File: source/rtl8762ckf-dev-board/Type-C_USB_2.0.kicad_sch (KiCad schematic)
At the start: 14 parts, among them J10 USB_C_Receptacle_USB2.0, U3 USBLC6-2SC6

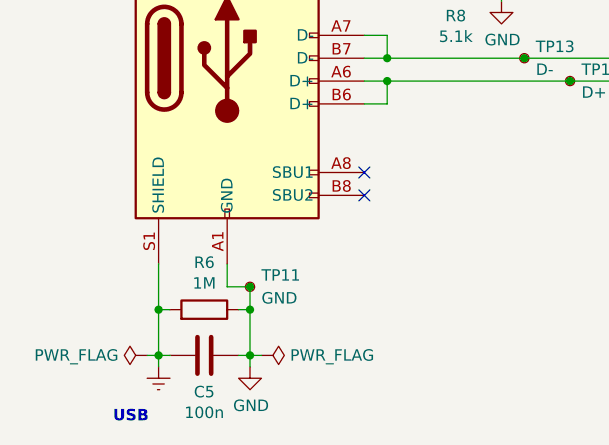
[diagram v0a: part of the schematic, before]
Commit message: implemented pico probe
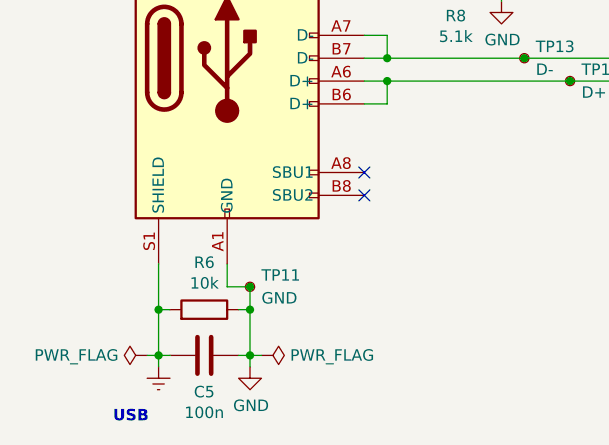
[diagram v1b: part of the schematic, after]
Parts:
- C5, C6: LCSC (none) -> C1546; MPN (none) -> 0402CG101J500NT
- C7: LCSC (none) -> C15525; MPN (none) -> CL05A106MQ5NUNC
- F1: LCSC C914092 -> C124083; MPN BSMD0603-075-6V -> BSMD0402L-050
- FB1: footprint Inductor_SMD:L_0402_1005Metric -> Inductor_SMD:L_0603_1608Metric; MPN UPZ1608E601-2R0TF -> CBW100505U601T
- J10: LCSC C2848615 -> C2927039; MPN TYPE-C-31-D-09 -> USB-TYPE-C-019
- R6: value 1M -> 10k; LCSC (none) -> C25086; MPN (none) -> 0402WGF100KTCE
- R7, R8: LCSC (none) -> C25905; MPN (none) -> 0402WGF5101TCE
- U3: LCSC (none) -> C2687116; MPN (none) -> USBLC6-2SC6
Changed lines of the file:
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@@
       (project "rtl8762ckf-dev-board"
         (path "/5477044b-5ae5-4ed6-bb7d-f5f3cc95a2d4/b26c93f0-3164-4866-a133-0e94099f2b64"
-          (reference "#PWR010") (unit 1)
+          (reference "#PWR027") (unit 1)
         )
       )
@@
       (effects (font (size 1.27 1.27)) hide)
     )
-    (property "Datasheet" "https://www.usb.org/sites/default/files/documents/usb_type-c.zip" (at 39.37 43.18 0)
-      (effects (font (size 1.27 1.27)) hide)
-    )
-    (property "LCSC" "C2848615" (at 35.56 43.18 0)
-      (effects (font (size 1.27 1.27)) hide)
-    )
-    (property "MPN" "TYPE-C-31-D-09" (at 35.56 43.18 0)
+    (property "Datasheet" "https://datasheet.lcsc.com/lcsc/2201121330_DEALON-USB-TYPE-C-019_C2927039.pdf" (at 39.37 43.18 0)
+      (effects (font (size 1.27 1.27)) hide)
+    )
+    (property "LCSC" "C2927039" (at 35.56 43.18 0)
+      (effects (font (size 1.27 1.27)) hide)
+    )
+    (property "MPN" "USB-TYPE-C-019" (at 35.56 43.18 0)
       (effects (font (size 1.27 1.27)) hide)
     )
@@
       (project "rtl8762ckf-dev-board"
         (path "/5477044b-5ae5-4ed6-bb7d-f5f3cc95a2d4/b26c93f0-3164-4866-a133-0e94099f2b64"
-          (reference "J2") (unit 1)
+          (reference "J7") (unit 1)
         )
       )
@@
       (effects (font (size 1.27 1.27)) hide)
     )
-    (property "Datasheet" "http://www2.st.com/resource/en/datasheet/CD00050750.pdf" (at 100.33 53.34 0)
+    (property "Datasheet" "http://www2.st.com/resource/en/datasheet/CD00050750.https://datasheet.lcsc.com/lcsc/2206231215_UMW-Youtai-Semiconductor-Co---Ltd--USBLC6-2SC6_C2687116.pdf" (at 100.33 53.34 0)
+      (effects (font (size 1.27 1.27)) hide)
+    )
+    (property "LCSC" "C2687116" (at 109.22 58.42 0)
+      (effects (font (size 1.27 1.27)) hide)
+    )
+    (property "MPN" "USBLC6-2SC6" (at 109.22 58.42 0)
       (effects (font (size 1.27 1.27)) hide)
     )
@@
       (project "rtl8762ckf-dev-board"
         (path "/5477044b-5ae5-4ed6-bb7d-f5f3cc95a2d4/b26c93f0-3164-4866-a133-0e94099f2b64"
-          (reference "U2") (unit 1)
+          (reference "U3") (unit 1)
         )
       )
@@
       (project "rtl8762ckf-dev-board"
         (path "/5477044b-5ae5-4ed6-bb7d-f5f3cc95a2d4/b26c93f0-3164-4866-a133-0e94099f2b64"
-          (reference "#PWR013") (unit 1)
+          (reference "#PWR030") (unit 1)
         )
       )
@@
       (project "rtl8762ckf-dev-board"
         (path "/5477044b-5ae5-4ed6-bb7d-f5f3cc95a2d4/b26c93f0-3164-4866-a133-0e94099f2b64"
-          (reference "#PWR08") (unit 1)
+          (reference "#PWR025") (unit 1)
         )
       )
@@
       (project "rtl8762ckf-dev-board"
         (path "/5477044b-5ae5-4ed6-bb7d-f5f3cc95a2d4/b26c93f0-3164-4866-a133-0e94099f2b64"
-          (reference "#PWR07") (unit 1)
+          (reference "#PWR024") (unit 1)
         )
       )
@@
       (effects (font (size 1.27 1.27)))
     )
-    (property "Value" "1M" (at 33.02 68.193 90)
+    (property "Value" "10k" (at 33.02 68.193 90)
       (effects (font (size 1.27 1.27)))
     )
@@
       (effects (font (size 1.27 1.27)) hide)
     )
-    (property "Datasheet" "~" (at 33.02 71.12 0)
+    (property "Datasheet" "https://datasheet.lcsc.com/lcsc/2205311900_UNI-ROYAL-Uniroyal-Elec-0402WGF100KTCE_C25086.pdf" (at 33.02 71.12 0)
+      (effects (font (size 1.27 1.27)) hide)
+    )
+    (property "LCSC" "C25086" (at 33.02 71.12 0)
+      (effects (font (size 1.27 1.27)) hide)
+    )
+    (property "MPN" "0402WGF100KTCE" (at 33.02 71.12 0)
       (effects (font (size 1.27 1.27)) hide)
     )
@@
       (project "rtl8762ckf-dev-board"
         (path "/5477044b-5ae5-4ed6-bb7d-f5f3cc95a2d4/b26c93f0-3164-4866-a133-0e94099f2b64"
-          (reference "R1") (unit 1)
+          (reference "R5") (unit 1)
         )
       )
@@
       (effects (font (size 1.27 1.27)) hide)
     )
+    (property "LCSC" "C25905" (at 60.96 35.56 0)
+      (effects (font (size 1.27 1.27)) hide)
+    )
+    (property "MPN" "0402WGF5101TCE" (at 60.96 35.56 0)
+      (effects (font (size 1.27 1.27)) hide)
+    )
     (pin "1")
     (pin "2")
@@
       (project "rtl8762ckf-dev-board"
         (path "/5477044b-5ae5-4ed6-bb7d-f5f3cc95a2d4/b26c93f0-3164-4866-a133-0e94099f2b64"
-          (reference "R3") (unit 1)
+          (reference "R7") (unit 1)
         )
       )
@@
       (effects (font (size 1.27 1.27)) hide)
     )
+    (property "LCSC" "C15525" (at 99.06 30.48 0)
+      (effects (font (size 1.27 1.27)) hide)
+    )
+    (property "MPN" "CL05A106MQ5NUNC" (at 99.06 30.48 0)
+      (effects (font (size 1.27 1.27)) hide)
+    )
     (pin "1")
     (pin "2")
@@
       (project "rtl8762ckf-dev-board"
         (path "/5477044b-5ae5-4ed6-bb7d-f5f3cc95a2d4/b26c93f0-3164-4866-a133-0e94099f2b64"
-          (reference "C19") (unit 1)
+          (reference "C22") (unit 1)
         )
       )
@@
       (effects (font (size 1.27 1.27)))
     )
-    (property "Footprint" "Inductor_SMD:L_0402_1005Metric" (at 93.98 23.622 90)
-      (effects (font (size 1.27 1.27)) hide)
-    )
-    (property "Datasheet" "https://www.sunlordinc.com/UploadFiles/PDF_Cat/20110524142806261.pdf" (at 93.98 25.4 0)
-      (effects (font (size 1.27 1.27)) hide)
-    )
-    (property "MPN" "UPZ1608E601-2R0TF" (at 93.98 25.4 90)
+    (property "Footprint" "Inductor_SMD:L_0603_1608Metric" (at 93.98 23.622 90)
+      (effects (font (size 1.27 1.27)) hide)
+    )
+    (property "Datasheet" "https://datasheet.lcsc.com/lcsc/1811141730_FH--Guangdong-Fenghua-Advanced-Tech-CBW100505U601T_C124083.pdf" (at 93.98 25.4 0)
+      (effects (font (size 1.27 1.27)) hide)
+    )
+    (property "MPN" "CBW100505U601T" (at 93.98 25.4 90)
       (effects (font (size 1.27 1.27)) hide)
     )
@@
       (effects (font (size 1.27 1.27)) hide)
     )
+    (property "LCSC" "C1546" (at 33.02 76.2 0)
+      (effects (font (size 1.27 1.27)) hide)
+    )
+    (property "MPN" "0402CG101J500NT" (at 33.02 76.2 0)
+      (effects (font (size 1.27 1.27)) hide)
+    )
     (pin "1")
     (pin "2")
@@
       (project "rtl8762ckf-dev-board"
         (path "/5477044b-5ae5-4ed6-bb7d-f5f3cc95a2d4/b26c93f0-3164-4866-a133-0e94099f2b64"
-          (reference "C17") (unit 1)
+          (reference "C20") (unit 1)
         )
       )
@@
       (project "rtl8762ckf-dev-board"
         (path "/5477044b-5ae5-4ed6-bb7d-f5f3cc95a2d4/b26c93f0-3164-4866-a133-0e94099f2b64"
-          (reference "#PWR09") (unit 1)
+          (reference "#PWR026") (unit 1)
         )
       )
@@
       (effects (font (size 1.27 1.27)) hide)
     )
+    (property "LCSC" "C1546" (at 93.98 63.5 0)
+      (effects (font (size 1.27 1.27)) hide)
+    )
+    (property "MPN" "0402CG101J500NT" (at 93.98 63.5 0)
+      (effects (font (size 1.27 1.27)) hide)
+    )
     (pin "1")
     (pin "2")
@@
       (project "rtl8762ckf-dev-board"
         (path "/5477044b-5ae5-4ed6-bb7d-f5f3cc95a2d4/b26c93f0-3164-4866-a133-0e94099f2b64"
-          (reference "C18") (unit 1)
+          (reference "C21") (unit 1)
         )
       )
@@
       (project "rtl8762ckf-dev-board"
         (path "/5477044b-5ae5-4ed6-bb7d-f5f3cc95a2d4/b26c93f0-3164-4866-a133-0e94099f2b64"
-          (reference "#PWR011") (unit 1)
+          (reference "#PWR028") (unit 1)
         )
       )
@@
       (effects (font (size 1.27 1.27)) (justify left) hide)
     )
-    (property "Datasheet" "https://datasheet.lcsc.com/lcsc/1809292114_TLC-Electronic-TLC-FSMD020_C261935.pdf" (at 76.2 25.4 0)
-      (effects (font (size 1.27 1.27)) hide)
-    )
-    (property "MPN" "BSMD0603-075-6V" (at 76.2 25.4 90)
-      (effects (font (size 1.27 1.27)) hide)
-    )
-    (property "LCSC" "C914092" (at 76.2 25.4 90)
+    (property "Datasheet" "https://datasheet.lcsc.com/lcsc/2203021130_BHFUSE-BSMD0402L-050_C914087.pdf" (at 76.2 25.4 0)
+      (effects (font (size 1.27 1.27)) hide)
+    )
+    (property "MPN" "BSMD0402L-050" (at 76.2 25.4 90)
+      (effects (font (size 1.27 1.27)) hide)
+    )
+    (property "LCSC" "C124083" (at 76.2 25.4 90)
       (effects (font (size 1.27 1.27)) hide)
     )
@@
       (project "rtl8762ckf-dev-board"
         (path "/5477044b-5ae5-4ed6-bb7d-f5f3cc95a2d4/b26c93f0-3164-4866-a133-0e94099f2b64"
-          (reference "#PWR012") (unit 1)
+          (reference "#PWR029") (unit 1)
         )
       )
@@
       (project "rtl8762ckf-dev-board"
         (path "/5477044b-5ae5-4ed6-bb7d-f5f3cc95a2d4/b26c93f0-3164-4866-a133-0e94099f2b64"
-          (reference "#PWR05") (unit 1)
+          (reference "#PWR022") (unit 1)
         )
       )
@@
       (project "rtl8762ckf-dev-board"
         (path "/5477044b-5ae5-4ed6-bb7d-f5f3cc95a2d4/b26c93f0-3164-4866-a133-0e94099f2b64"
-          (reference "#PWR06") (unit 1)
+          (reference "#PWR023") (unit 1)
         )
       )
@@
       (effects (font (size 1.27 1.27)) hide)
     )
+    (property "LCSC" "C25905" (at 60.96 33.02 0)
+      (effects (font (size 1.27 1.27)) hide)
+    )
+    (property "MPN" "0402WGF5101TCE" (at 60.96 33.02 0)
+      (effects (font (size 1.27 1.27)) hide)
+    )
     (pin "1")
     (pin "2")
@@
       (project "rtl8762ckf-dev-board"
         (path "/5477044b-5ae5-4ed6-bb7d-f5f3cc95a2d4/b26c93f0-3164-4866-a133-0e94099f2b64"
-          (reference "R2") (unit 1)
-        )
-      )
+          (reference "R6") (unit 1)
+        )
+      )

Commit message: set correct PNs for R5, R8, R11; closes #5
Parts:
- R6: LCSC C25086 -> C25744; MPN 0402WGF100KTCE -> 0402WGF1002TCE
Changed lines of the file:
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@@
       (effects (font (size 1.27 1.27)) hide)
     )
-    (property "LCSC" "C25086" (at 33.02 71.12 0)
+    (property "LCSC" "C25744" (at 33.02 71.12 0)
       (effects (font (size 1.27 1.27)) hide)
     )
-    (property "MPN" "0402WGF100KTCE" (at 33.02 71.12 0)
+    (property "MPN" "0402WGF1002TCE" (at 33.02 71.12 0)
       (effects (font (size 1.27 1.27)) hide)
     )
